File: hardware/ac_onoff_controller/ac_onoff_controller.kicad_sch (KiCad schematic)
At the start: 20 parts, among them M1 Motor_Servo, Q1 S8050, Q2 S8050, Q3 2SC1815, Q4 S8050, SW1 SW_Push, SW2 SW_Push, U1 ATmega88P-20P, U2 DHT11

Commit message: add pcb
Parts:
- removed R5: 5.1k, Resistor_THT:R_Axial_DIN0309_L9.0mm_D3.2mm_P15.24mm_Horizontal, symbol Device:R
- added C5: 0.1u, Capacitor_THT:C_Disc_D4.3mm_W1.9mm_P5.00mm, symbol Device:C
- added D2: 1N4148, Diode_THT:D_A-405_P10.16mm_Horizontal, symbol Device:D
- added J1: Conn_02x04_Odd_Even, Connector_PinHeader_2.54mm:PinHeader_2x03_P2.54mm_Vertical, symbol Connector_Generic:Conn_02x03_Odd_Even
- added J2: Conn_01x02, Connector_PinHeader_2.54mm:PinHeader_1x02_P2.54mm_Vertical, symbol Connector_Generic:Conn_01x02
- added SW3: SW_SPST, Connector_JST:JST_XH_B2B-XH-AM_1x02_P2.50mm_Vertical, symbol Switch:SW_SPST
- C1: footprint Capacitor_THT:CP_Radial_D24.0mm_P10.00mm_3pin_SnapIn -> Capacitor_THT:C_Disc_D4.3mm_W1.9mm_P5.00mm
- Q1, Q2, Q3, Q4: footprint Package_TO_SOT_THT:TO-92_Inline -> Package_TO_SOT_THT:TO-92_Inline_Wide
- R1: footprint Resistor_THT:R_Axial_Power_L38.0mm_W9.0mm_P45.72mm -> Resistor_THT:R_Axial_DIN0309_L9.0mm_D3.2mm_P15.24mm_Horizontal
- R4: footprint Resistor_THT:R_Axial_DIN0309_L9.0mm_D3.2mm_P15.24mm_Horizontal -> Resistor_THT:R_Axial_DIN0207_L6.3mm_D2.5mm_P2.54mm_Vertical
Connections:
- net GND: now also J1.6 (Pin_6), J2.2 (Pin_2)
- net VCC: now also C5.1, D2.1 (K), J1.2 (Pin_2)
- net at M1.3 (-), Q2.3 (C): now also C5.2, D2.2 (A)
- net RST: now reaches U1.1 (~{RESET}/PC6)
- net RST: now also J1.5 (Pin_5)
- net MOSI: now reaches U1.17 (PB3)
- net MOSI: now also J1.4 (Pin_4)
- net MISO: now reaches U1.18 (PB4)
- net MISO: now also J1.1 (Pin_1)
- net SCK: now reaches U1.19 (PB5)
- net SCK: now also J1.3 (Pin_3)
- net at U1.3 (PD1): now also J2.1 (Pin_1)
- net at Q1.3 (C), Q4.3 (C), R1.1: now also SW3.2 (B); no longer BT1.1 (+)
- new net: BT1.1 (+), SW3.1 (A)
- no-connect marks 20 -> 15
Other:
- note added: "IR2↓"
- note added: "I_{OUT} →"
- note added: "← I^{Q3}_{B}"
- note added: "↑I^{Q4}_{B}"
- note added: "↓I^{Q3}_C"
- note added: "↓I_{D1}"
- note added: "↓I_{R1}"
- note added: "↥V_{D1}"
- note added: "↥V_{R3}"
- moved on the sheet: C2, Q2, R4, SW1, SW2

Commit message: wip: modify footprints etc. for ordering PCBs
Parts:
- removed Q1, Q2, Q4: S8050, Package_TO_SOT_THT:TO-92_Inline_Wide, symbol Transistor_BJT:S8050
- added C6: 0.1u, Capacitor_THT:C_Disc_D4.3mm_W1.9mm_P5.00mm, symbol Device:C
- added D3: 1N4148, Diode_THT:D_A-405_P10.16mm_Horizontal, symbol Device:D
- added D4, D5, D6: LED, LED_THT:LED_D3.0mm, symbol Device:LED
- added M2: Motor_Servo, Connector_PinHeader_2.54mm:PinHeader_1x03_P2.54mm_Vertical, symbol Motor:Motor_Servo
- added Q1, Q2, Q6: 2SK4017, Package_TO_SOT_THT:TO-251-3-1EP_Horizontal_TabDown, symbol Device:Q_NMOS_GDS
- added R5: 500, Resistor_THT:R_Axial_DIN0207_L6.3mm_D2.5mm_P2.54mm_Vertical, symbol Device:R
- added SW4: SW_Push, Button_Switch_THT:SW_PUSH_6mm_H7.3mm, symbol Switch:SW_Push
- BT1: footprint Connector_JST:JST_XH_B2B-XH-AM_1x02_P2.50mm_Vertical -> Connector_JST:JST_XH_B4B-XH-A_1x04_P2.50mm_Vertical; purchase (none) -> 0
- C1, C2, C3, C4, C5, D1, D2, J1, J2, Q3, R1, R2, R3, R4, SW1, SW2, U1: purchase (none) -> 0
- M1: footprint Connector_JST:JST_XH_B3B-XH-AM_1x03_P2.50mm_Vertical -> Connector_PinHeader_2.54mm:PinHeader_1x03_P2.54mm_Vertical; purchase (none) -> 0
- SW3: footprint Connector_JST:JST_XH_B2B-XH-AM_1x02_P2.50mm_Vertical -> ac_onoff_controller:SS-22F25-G4; symbol Switch:SW_SPST -> Switch:SW_SPDT; MPN (none) -> SS-22F25-G4; URL (none) -> https://eleshop.jp/shop/g/gJ43315/; purchase (none) -> 0
- U2: purchase (none) -> 1
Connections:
- net GND: now also D4.1 (K), D5.1 (K), D6.1 (K), Q1.3 (S), Q2.3 (S), SW4.2
- net RST: now also SW4.1
- net VCC: now also C6.1, D3.1 (K), M2.2 (+), Q6.3 (S)
- net at R4.2: now also Q1.1 (G)
- net at C5.2, D2.2 (A), M1.3 (-): now also Q1.2 (D)
- net at R4.1, U1.16 (PB2): now also R5.1
- net PC0: now reaches U1.23 (PC0)
- net PC0: now also M2.1 (PWM)
- net STON: now reaches U1.4 (PD2)
- net STON: now also D4.2 (A)
- net STOFF: now reaches U1.5 (PD3)
- net STOFF: now also D5.2 (A)
- net TGL: now reaches U1.6 (PD4)
- net TGL: now also D6.2 (A)
- net at C1.1, Q3.2 (C), R1.2: now also Q6.1 (G)
- net at SW3.1 (A): now also R1.1, Q6.2 (D); no longer BT1.1 (+)
- net at SW3.2 (B): now also BT1.1 (+); no longer R1.1
- new net: Q2.1 (G), R5.2
- new net: C6.2, D3.2 (A), M2.3 (-), Q2.2 (D)
- no-connect marks 15 -> 12
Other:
- moved on the sheet: U1

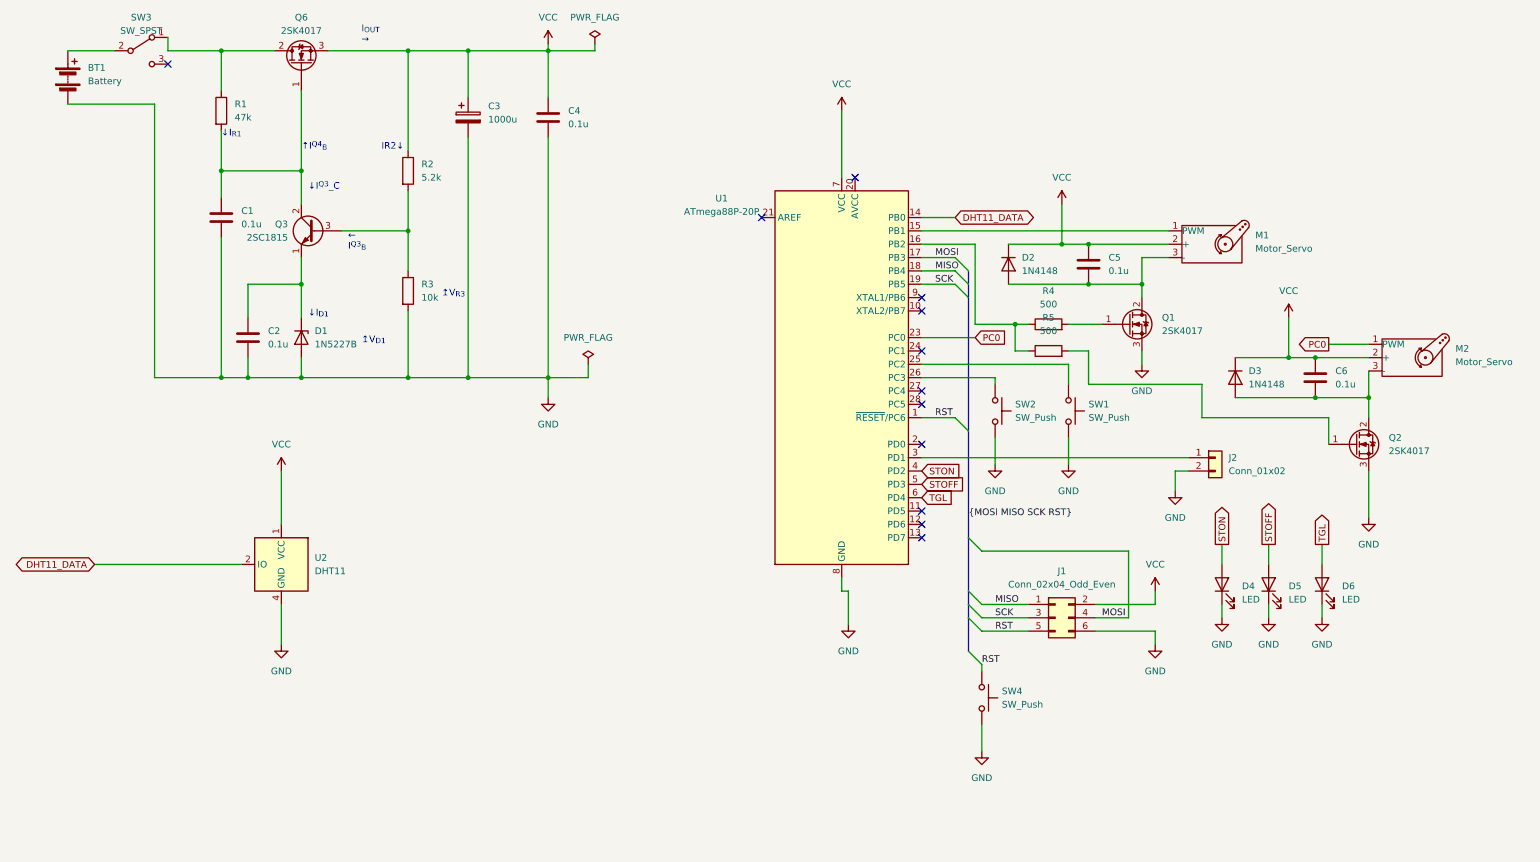
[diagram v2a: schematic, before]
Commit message: modify footprints etc. for ordering PCBs
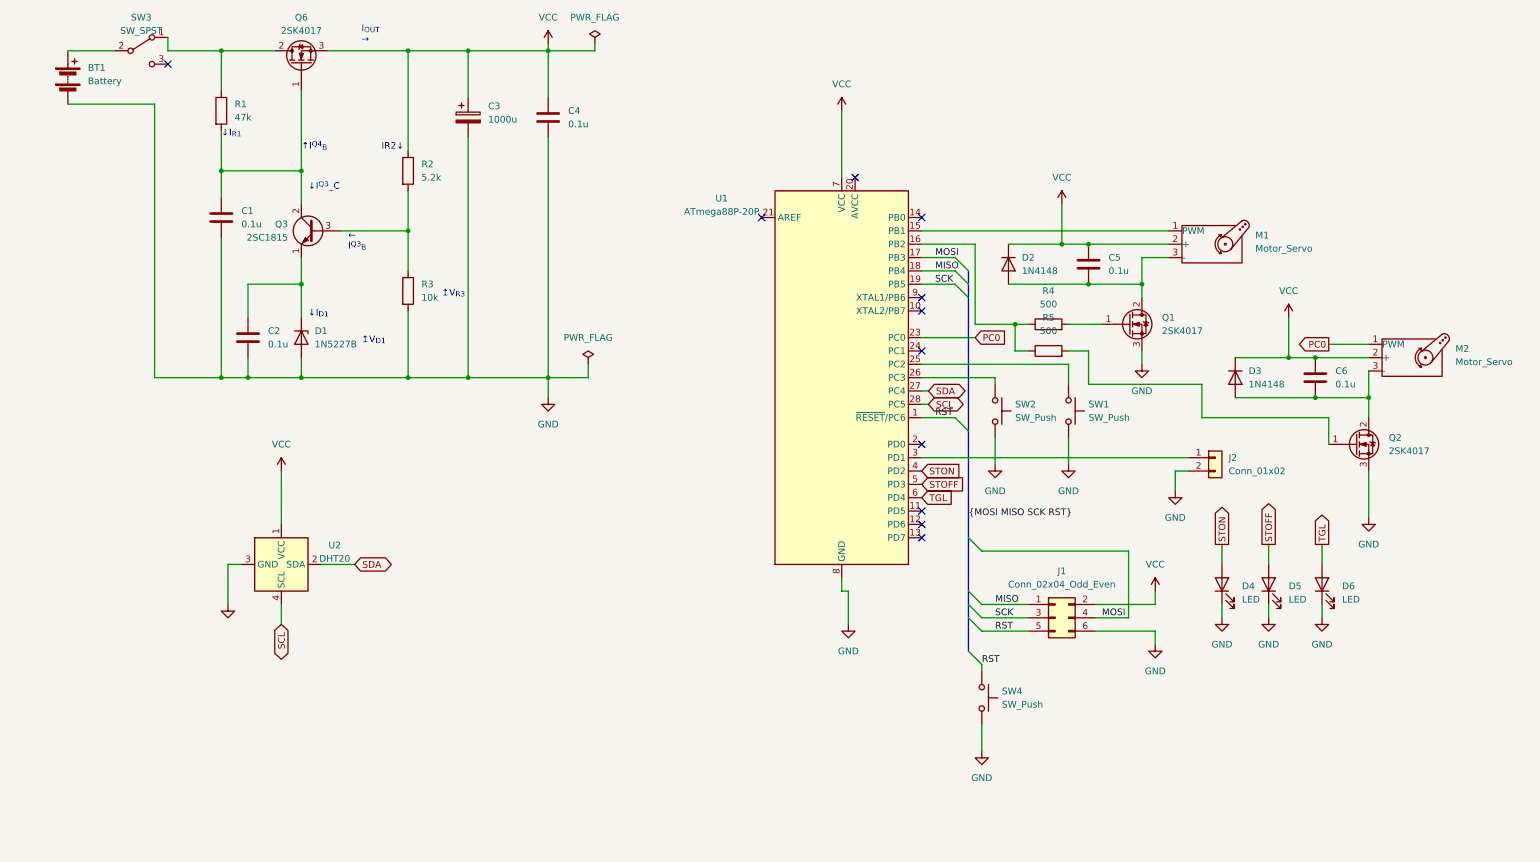
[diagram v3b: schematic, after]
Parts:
- removed U2: DHT11, Sensor:Aosong_DHT11_5.5x12.0_P2.54mm, symbol Sensor:DHT11
- added U2: DHT20, ac_onoff_controller:Aosong_DHT20, symbol ac_onoff_controller:DHT20
- BT1: symbol Device:Battery -> ac_onoff_controller:Battery_2Pins_OutOf_4Pins
- Q1, Q2, Q6: footprint Package_TO_SOT_THT:TO-251-3-1EP_Horizontal_TabDown -> ac_onoff_controller:2SK4017
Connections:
- net GND: now also U2.3 (GND)
- net VCC: now also U2.1 (VCC)
- net SDA: now reaches U1.27 (PC4)
- net SDA: now also U2.2 (SDA)
- net SCL: now reaches U1.28 (PC5)
- net SCL: now also U2.4 (SCL)
- net DHT11_DATA: no longer names the net of U1.14 (PB0)
- no-connect marks 12 -> 11
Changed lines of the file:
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@@
   (no_connect (at 196.85 130.81))
   (no_connect (at 196.85 87.63))
+  (no_connect (at 196.85 72.39))
   (no_connect (at 184.15 64.77))
-  (no_connect (at 196.85 107.95))
   (no_connect (at 196.85 133.35))
   (no_connect (at 166.37 72.39))
@@
   (no_connect (at 196.85 128.27))
   (no_connect (at 196.85 90.17))
-  (no_connect (at 196.85 105.41))
   (no_connect (at 196.85 115.57))
   (bus_entry (at 203.2 80.01) (size 2.54 2.54)
@@
     (stroke (width 0) (type default))
   )
+  (wire (pts (xy 74.93 146.05) (xy 74.93 149.86))
+    (stroke (width 0) (type default))
+  )
   (wire (pts (xy 125.73 102.87) (xy 125.73 106.68))
     (stroke (width 0) (type default))
@@
     (stroke (width 0) (type default))
   )
+  (wire (pts (xy 196.85 107.95) (xy 198.12 107.95))
+    (stroke (width 0) (type default))
+  )
   (wire (pts (xy 238.76 80.01) (xy 243.84 80.01))
     (stroke (width 0) (type default))
@@
     (stroke (width 0) (type default))
   )
-  (wire (pts (xy 74.93 146.05) (xy 74.93 153.67))
+  (wire (pts (xy 64.77 138.43) (xy 64.77 146.05))
     (stroke (width 0) (type default))
   )
@@
     (stroke (width 0) (type default))
   )
-  (wire (pts (xy 39.37 138.43) (xy 67.31 138.43))
+  (wire (pts (xy 64.77 138.43) (xy 67.31 138.43))
     (stroke (width 0) (type default))
   )
@@
     (stroke (width 0) (type default))
   )
+  (wire (pts (xy 196.85 105.41) (xy 198.12 105.41))
+    (stroke (width 0) (type default))
+  )
   (wire (pts (xy 274.32 115.57) (xy 274.32 110.49))
     (stroke (width 0) (type default))
@@
     (stroke (width 0) (type default))
   )
+  (wire (pts (xy 82.55 138.43) (xy 88.9 138.43))
+    (stroke (width 0) (type default))
+  )
   (bus (pts (xy 205.74 143.51) (xy 205.74 146.05))
     (stroke (width 0) (type default))
@@
   )
   (wire (pts (xy 207.01 77.47) (xy 207.01 92.71))
-    (stroke (width 0) (type default))
-  )
-  (wire (pts (xy 196.85 72.39) (xy 203.2 72.39))
     (stroke (width 0) (type default))
   )
@@
   (label "RST" (at 210.82 151.13 0) (fields_autoplaced)
     (effects (font (size 1.27 1.27)) (justify left bottom))
+  )
+  (global_label "SDA" (shape bidirectional) (at 88.9 138.43 0) (fields_autoplaced)
+    (effects (font (size 1.27 1.27)) (justify left))
+    (property "Intersheetrefs" "${INTERSHEET_REFS}" (at 96.5646 138.43 0)
+      (effects (font (size 1.27 1.27)) (justify left) hide)
+    )
   )
   (global_label "TGL" (shape output) (at 273.05 134.62 90) (fields_autoplaced)
@@
     )
   )
-  (global_label "DHT11_DATA" (shape bidirectional) (at 39.37 138.43 180) (fields_autoplaced)
-    (effects (font (size 1.27 1.27)) (justify right))
-    (property "Intersheetrefs" "${INTERSHEET_REFS}" (at 23.904 138.43 0)
-      (effects (font (size 1.27 1.27)) (justify right) hide)
+  (global_label "SDA" (shape bidirectional) (at 198.12 105.41 0) (fields_autoplaced)
+    (effects (font (size 1.27 1.27)) (justify left))
+    (property "Intersheetrefs" "${INTERSHEET_REFS}" (at 205.7846 105.41 0)
+      (effects (font (size 1.27 1.27)) (justify left) hide)
     )
   )
@@
     )
   )
-  (global_label "DHT11_DATA" (shape bidirectional) (at 203.2 72.39 0) (fields_autoplaced)
+  (global_label "SCL" (shape bidirectional) (at 198.12 107.95 0) (fields_autoplaced)
     (effects (font (size 1.27 1.27)) (justify left))
-    (property "Intersheetrefs" "${INTERSHEET_REFS}" (at 218.666 72.39 0)
+    (property "Intersheetrefs" "${INTERSHEET_REFS}" (at 205.7241 107.95 0)
       (effects (font (size 1.27 1.27)) (justify left) hide)
     )
@@
     )
   )
+  (global_label "SCL" (shape bidirectional) (at 74.93 149.86 270) (fields_autoplaced)
+    (effects (font (size 1.27 1.27)) (justify right))
+    (property "Intersheetrefs" "${INTERSHEET_REFS}" (at 74.93 157.4641 90)
+      (effects (font (size 1.27 1.27)) (justify right) hide)
+    )
+  )
   (global_label "STOFF" (shape input) (at 196.85 123.19 0) (fields_autoplaced)
     (effects (font (size 1.27 1.27)) (justify left))
@@
     (property "Intersheetrefs" "${INTERSHEET_REFS}" (at 262.89 125.95 90)
       (effects (font (size 1.27 1.27)) (justify left) hide)
-    )
-  )
-  (symbol (lib_id "Sensor:DHT11") (at 74.93 138.43 0) (mirror y) (unit 1)
-    (in_bom yes) (on_board yes) (dnp no) (fields_autoplaced)
-    (property "Reference" "U2" (at 81.28 137.16 0)
-      (effects (font (size 1.27 1.27)) (justify right))
-    )
-    (property "Value" "DHT11" (at 81.28 139.7 0)
-      (effects (font (size 1.27 1.27)) (justify right))
-    )
-    (property "Footprint" "Sensor:Aosong_DHT11_5.5x12.0_P2.54mm" (at 74.93 148.59 0)
-      (effects (font (size 1.27 1.27)) hide)
-    )
-    (property "Datasheet" "http://akizukidenshi.com/download/ds/aosong/DHT11.pdf" (at 71.12 132.08 0)
-      (effects (font (size 1.27 1.27)) hide)
-    )
-    (property "purchase" "1" (at 74.93 138.43 0)
-      (effects (font (size 1.27 1.27)) hide)
-    )
-    (pin "1")
-    (pin "2")
-    (pin "3")
-    (pin "4")
-    (instances
-      (project "ac_onoff_controller"
-        (path "/3fdcfeb5-507b-4398-9c86-207e73e94441"
-          (reference "U2") (unit 1)
-        )
-      )
     )
   )
@@
     )
   )
-  (symbol (lib_id "power:GND") (at 74.93 153.67 0) (unit 1)
-    (in_bom yes) (on_board yes) (dnp no) (fields_autoplaced)
-    (property "Reference" "#PWR09" (at 74.93 160.02 0)
-      (effects (font (size 1.27 1.27)) hide)
-    )
-    (property "Value" "GND" (at 74.93 158.75 0)
-      (effects (font (size 1.27 1.27)))
-    )
-    (property "Footprint" "" (at 74.93 153.67 0)
-      (effects (font (size 1.27 1.27)) hide)
-    )
-    (property "Datasheet" "" (at 74.93 153.67 0)
+  (symbol (lib_id "power:GND") (at 64.77 146.05 0) (unit 1)
+    (in_bom yes) (on_board yes) (dnp no) (fields_autoplaced)
+    (property "Reference" "#PWR09" (at 64.77 152.4 0)
+      (effects (font (size 1.27 1.27)) hide)
+    )
+    (property "Value" "GND" (at 64.77 151.13 0)
+      (effects (font (size 1.27 1.27)) hide)
+    )
+    (property "Footprint" "" (at 64.77 146.05 0)
+      (effects (font (size 1.27 1.27)) hide)
+    )
+    (property "Datasheet" "" (at 64.77 146.05 0)
       (effects (font (size 1.27 1.27)) hide)
     )
@@
       (effects (font (size 1.27 1.27)) (justify left))
     )
-    (property "Footprint" "Package_TO_SOT_THT:TO-251-3-1EP_Horizontal_TabDown" (at 284.48 113.03 0)
+    (property "Footprint" "ac_onoff_controller:2SK4017" (at 284.48 113.03 0)
       (effects (font (size 1.27 1.27)) hide)
     )
@@
     )
   )
+  (symbol (lib_id "ac_onoff_controller:DHT20") (at 74.93 138.43 0) (unit 1)
+    (in_bom yes) (on_board yes) (dnp no)
+    (property "Reference" "U2" (at 85.09 134.7821 0)
+      (effects (font (size 1.27 1.27)))
+    )
+    (property "Value" "DHT20" (at 85.09 137.3221 0)
+      (effects (font (size 1.27 1.27)))
+    )
+    (property "Footprint" "ac_onoff_controller:Aosong_DHT20" (at 74.93 148.59 0)
+      (effects (font (size 1.27 1.27)) hide)
+    )
+    (property "Datasheet" "" (at 78.74 132.08 0)
+      (effects (font (size 1.27 1.27)) hide)
+    )
+    (pin "1")
+    (pin "2")
+    (pin "3")
+    (pin "4")
+    (instances
+      (project "ac_onoff_controller"
+        (path "/3fdcfeb5-507b-4398-9c86-207e73e94441"
+          (reference "U2") (unit 1)
+        )
+      )
+    )
+  )
   (symbol (lib_id "power:GND") (at 182.88 149.86 0) (unit 1)
     (in_bom yes) (on_board yes) (dnp no) (fields_autoplaced)
@@
       (effects (font (size 1.27 1.27)) (justify left))
     )
-    (property "Footprint" "Package_TO_SOT_THT:TO-251-3-1EP_Horizontal_TabDown" (at 241.3 90.17 0)
+    (property "Footprint" "ac_onoff_controller:2SK4017" (at 241.3 90.17 0)
       (effects (font (size 1.27 1.27)) hide)
     )
@@
     )
   )
-  (symbol (lib_id "Device:Battery") (at 34.29 45.72 0) (unit 1)
+  (symbol (lib_id "ac_onoff_controller:Battery_2Pins_OutOf_4Pins") (at 34.29 45.72 0) (unit 1)
     (in_bom yes) (on_board yes) (dnp no) (fields_autoplaced)
     (property "Reference" "BT1" (at 38.1 43.8785 0)
@@
     (pin "1")
     (pin "2")
+    (pin "3")
+    (pin "4")
     (instances
       (project "ac_onoff_controller"
@@
       (effects (font (size 1.27 1.27)))
     )
-    (property "Footprint" "Package_TO_SOT_THT:TO-251-3-1EP_Horizontal_TabDown" (at 76.2 38.1 0)
-      (effects (font (size 1.27 1.27)) hide)
-    )
+    (property "Footprint" "ac_onoff_controller:2SK4017" (at 76.2 38.1 0)
+      (effects (font (size 1.27 1.27)) hide)
+    )

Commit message: wip: add a new pcb design for ordering to vendors
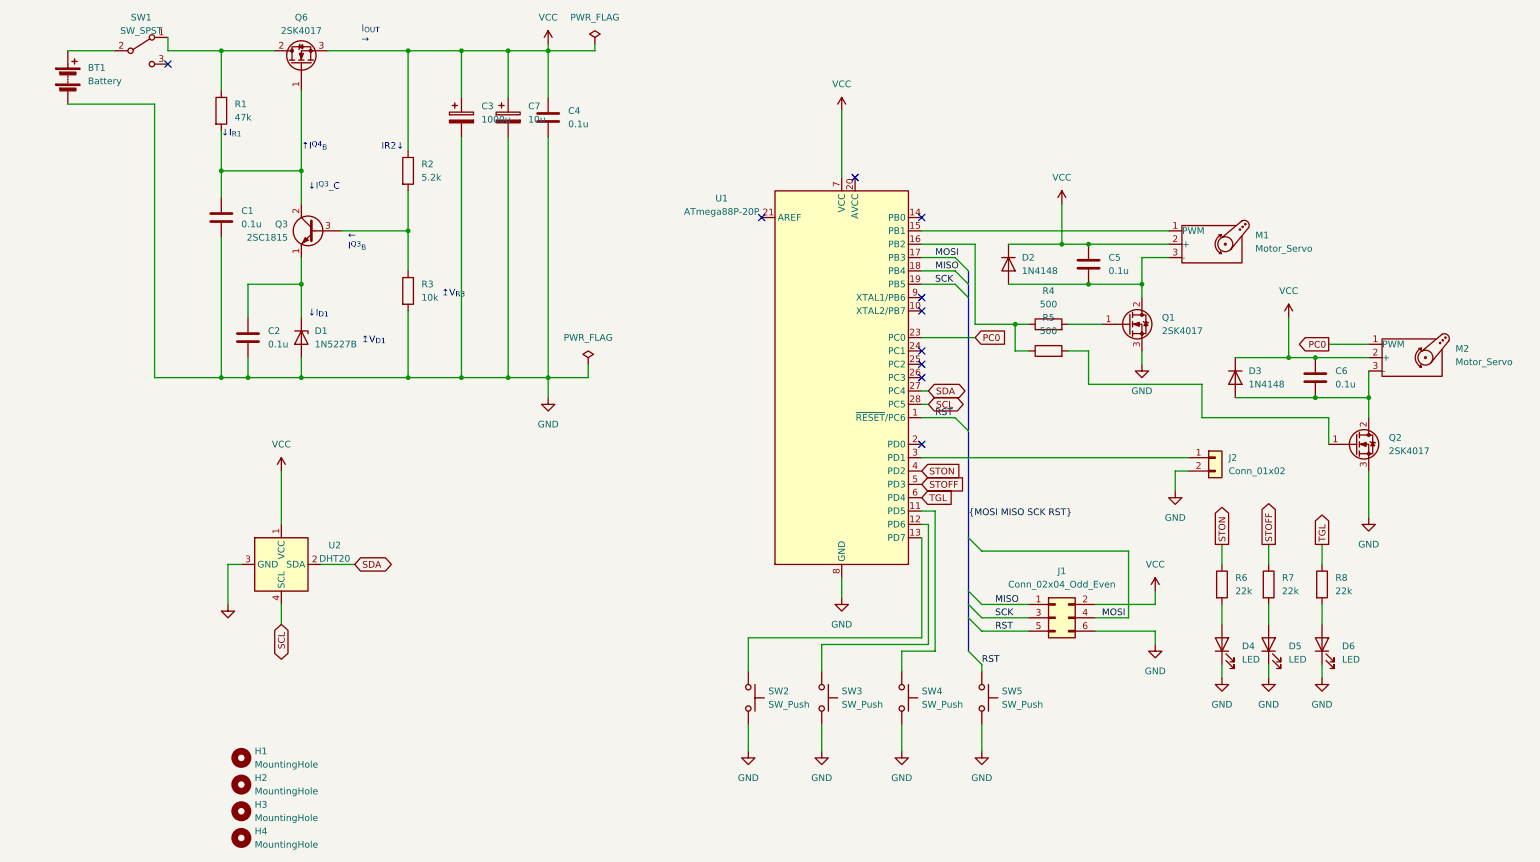
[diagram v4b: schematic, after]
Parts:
- added C7: 10u, Capacitor_THT:CP_Radial_D5.0mm_P2.00mm, symbol Device:C_Polarized
- added H1, H2, H3, H4: MountingHole, MountingHole:MountingHole_3.2mm_M3, symbol Mechanical:MountingHole
- added R6, R7, R8: 22k, Resistor_THT:R_Axial_DIN0309_L9.0mm_D3.2mm_P2.54mm_Vertical, symbol Device:R
- added SW4: SW_Push, Button_Switch_THT:SW_PUSH_6mm_H7.3mm, symbol Switch:SW_Push
- renumbered SW3 to SW1, SW1 to SW3, SW4 to SW5
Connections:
- net GND: now also C7.2, SW4.2
- net STOFF: now also R7.1; no longer D5.2 (A)
- net STON: now also R6.1; no longer D4.2 (A)
- net TGL: now also R8.1; no longer D6.2 (A)
- net VCC: now also C7.1
- net at U1.11 (PD5): now also SW4.1
- net at U1.12 (PD6): now also SW3.1
- net at U1.13 (PD7): now also SW2.1
- net at U1.25 (PC2): no longer SW3.1
- net at U1.26 (PC3): no longer SW2.1
- new net: D6.2 (A), R8.2
- new net: D5.2 (A), R7.2
- new net: D4.2 (A), R6.2
- no-connect marks 11 -> 10
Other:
- moved on the sheet: C3, D4, D5, D6, SW2, SW3
